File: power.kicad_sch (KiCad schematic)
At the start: 49 parts, among them IC1 STM32MP157AAB3, IC3 STC3117IJT, IC4 MCP73830T-2AAI_MYY, IC5 MT41K256M16TW-107_P, IC6 STPMIC1BPQR, P1 USB_C_Plug_USB2.0

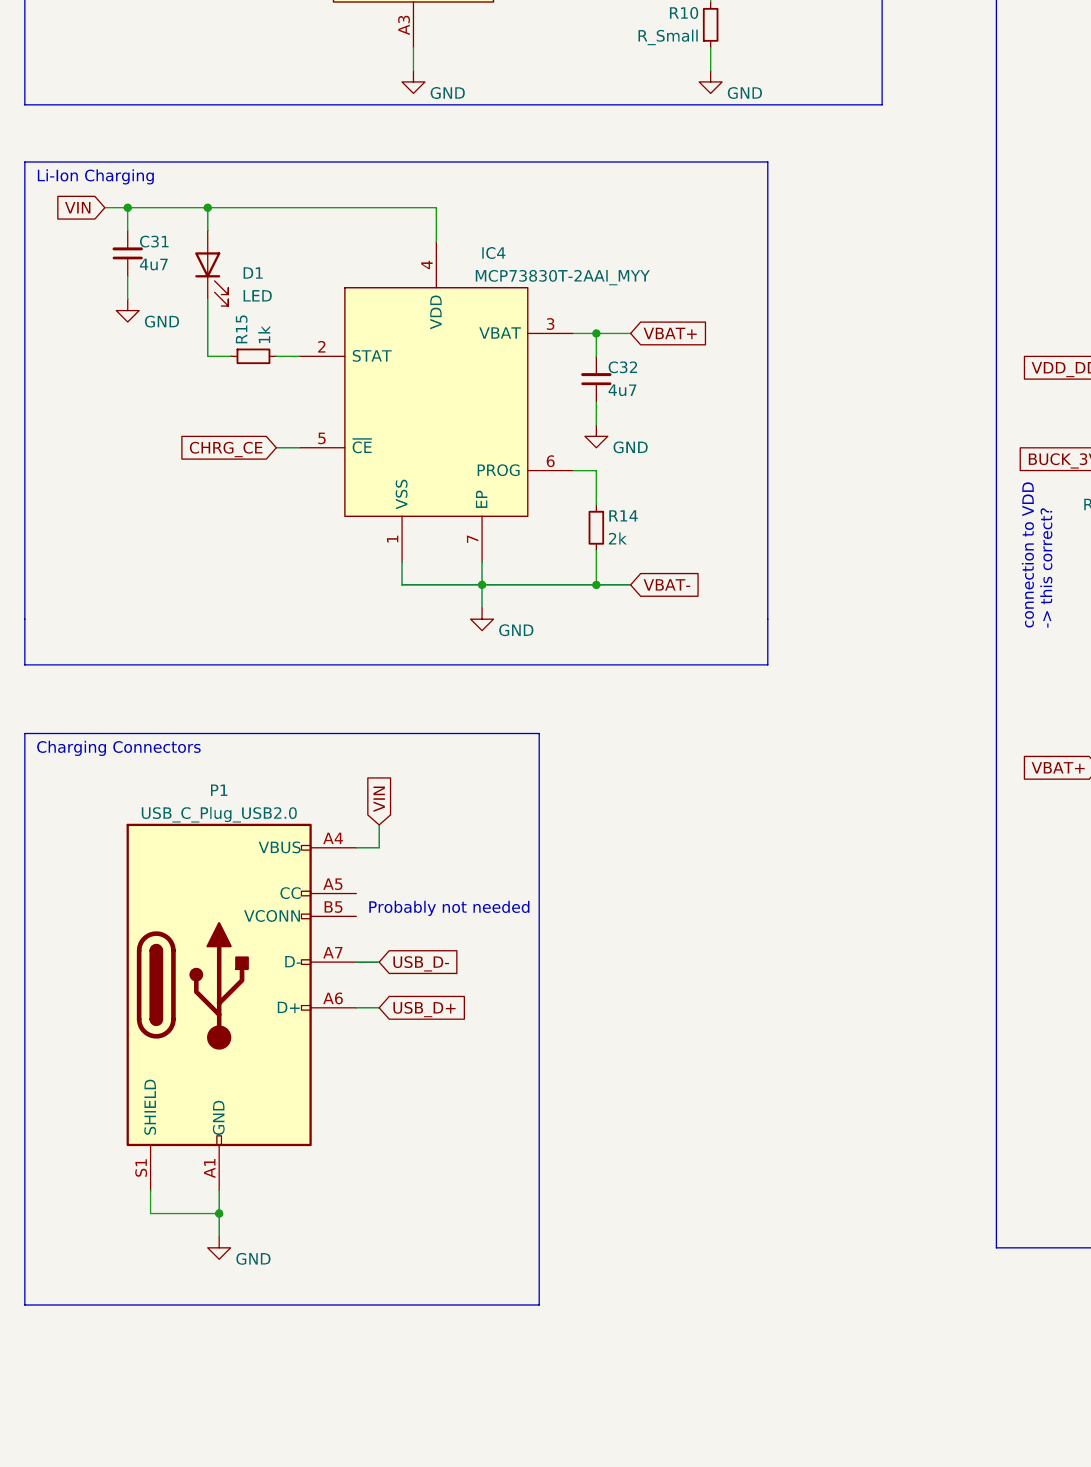
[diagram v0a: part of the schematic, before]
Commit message: Added Connectors
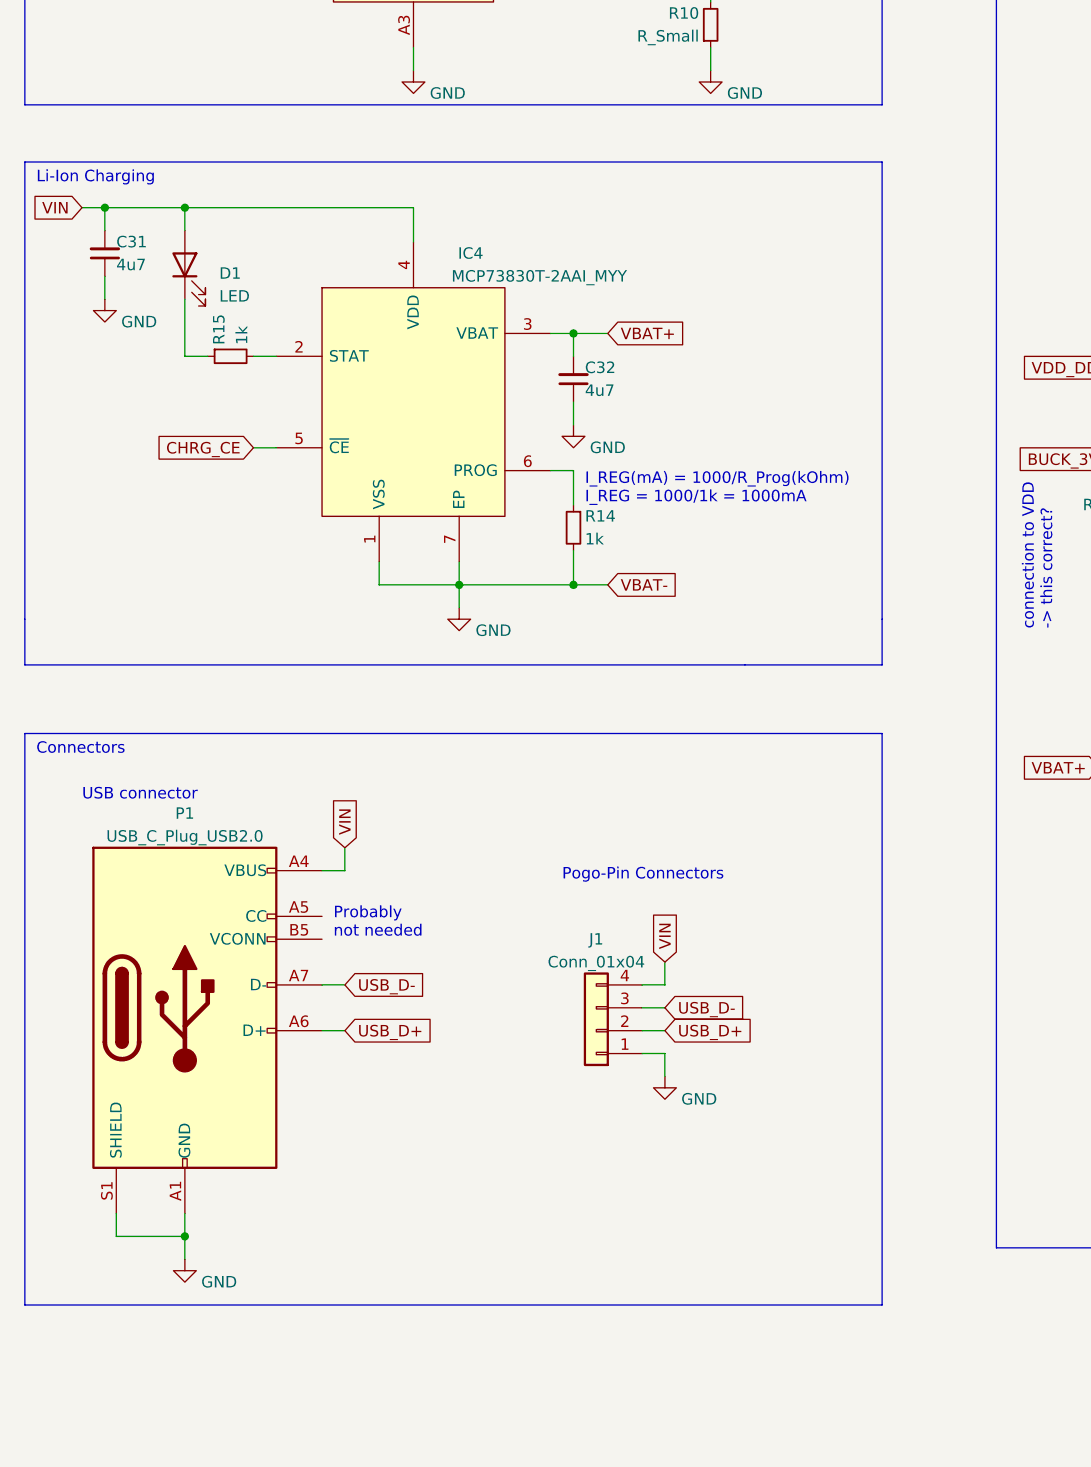
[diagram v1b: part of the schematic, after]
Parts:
- added J1: Conn_01x04, symbol Connector_Generic:Conn_01x04
- R14: value 2k -> 1k
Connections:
- net GND: now also J1.1 (Pin_1)
- net USB_D+: now also J1.2 (Pin_2)
- net USB_D-: now also J1.3 (Pin_3)
- net VIN: now also J1.4 (Pin_4)
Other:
- note added: "Connectors"
- note added: "I_REG(mA) = 1000/R_Prog(kOhm) I_REG = 1000/1k = 1000mA"
- note added: "Pogo-Pin Connectors"
- note added: "USB connector"
- note removed: "Charging Connectors"
- moved on the sheet: C31, C32, D1, IC4, P1, R14, R15

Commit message: Added STUSB1600A chip
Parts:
- added C33, C34, C35: 1u, Capacitor_SMD:C_0603_1608Metric, symbol Device:C_Small
- added C36: 10u, Capacitor_SMD:C_0603_1608Metric, symbol Device:C_Small
- added IC8: STUSB1600AQTR, ARMband:QFN50P400X400X100-25N, symbol ARMband:STUSB1600AQTR
- added R16, R18, R19, R22, R23, R24: 10k, Resistor_SMD:R_0603_1608Metric, symbol Device:R_Small
- added R17, R21: 1k, Resistor_SMD:R_0603_1608Metric, symbol Device:R_Small
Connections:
- net BUCK_3V3: now also C35.2, IC8.22 (VSYS), R18.2, R19.2, R22.2, R23.2, R24.2
- net GND: now also C33.1, C34.1, C35.1, C36.2, IC8.10 (GND), IC8.13 (ADDR0), IC8.25 (THERMAL_PAD), IC8.3 (VCONN), R21.2
- net SCL: now also IC8.7 (SCL)
- net SDA: now also IC8.8 (SDA)
- net VIN: now also C36.1, IC8.18 (VUS_SENSE)
- net USB_CC1: now reaches P1.A5 (CC)
- net USB_CC1: now also IC8.1 (CC1DB), IC8.2 (CC1)
- net USB_CC2: now reaches P1.B5 (VCONN)
- net USB_CC2: now also IC8.4 (CC2), IC8.5 (CC2DB)
- new net: R16.2, R17.1
- new net: IC8.19 (VBUS_EN_SNK), R17.2
- new net: C33.2, IC8.21 (VREG_1V2)
- new net: C34.2, IC8.23 (VREG_2V7)
- new net USB_ALERT#: IC8.9 (ALERT#), R23.1
- new net USB_ATTACH: IC8.12 (ATTACH), R19.1
- new net USB_A_B_SIDE: IC8.17 (A_B_SIDE), R24.1
- new net USB_DEBUG1: IC8.14 (DEBUG1), R18.1
- new net USB_RESET: IC8.6 (RESET), R21.1
- new net USB_VBUS_VALID: IC8.11 (VBUS_VALID), R22.1
- no-connect marks 0 -> 2
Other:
- note added: "STUSB in Sink application"
- note added: "TODO: dual PMOS"
- note added: "To GND/VIO"
- note added: "VIO: 3v3 or 1v8?"
- note added: "VSYS: power from system, connect to GND if not used"
- note removed: "Probably not needed"
- moved on the sheet: C10, C11, C12, C13, C14, C15, C16, C17, C18, C19, C20, C21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

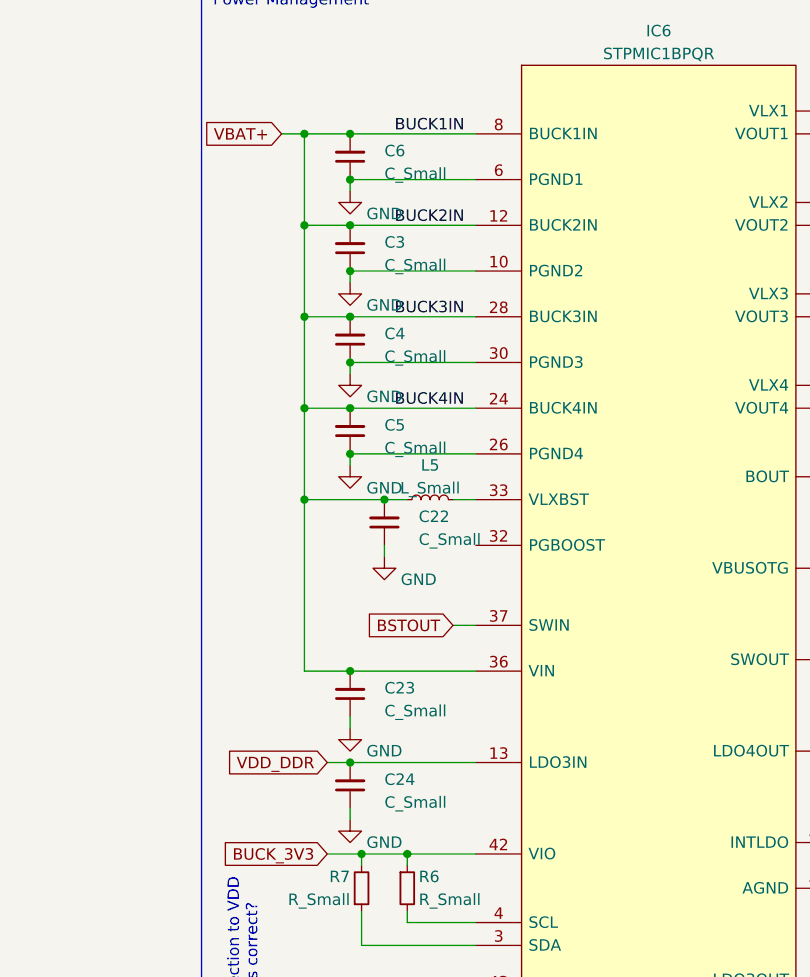
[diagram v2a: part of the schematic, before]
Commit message: added some part footprints
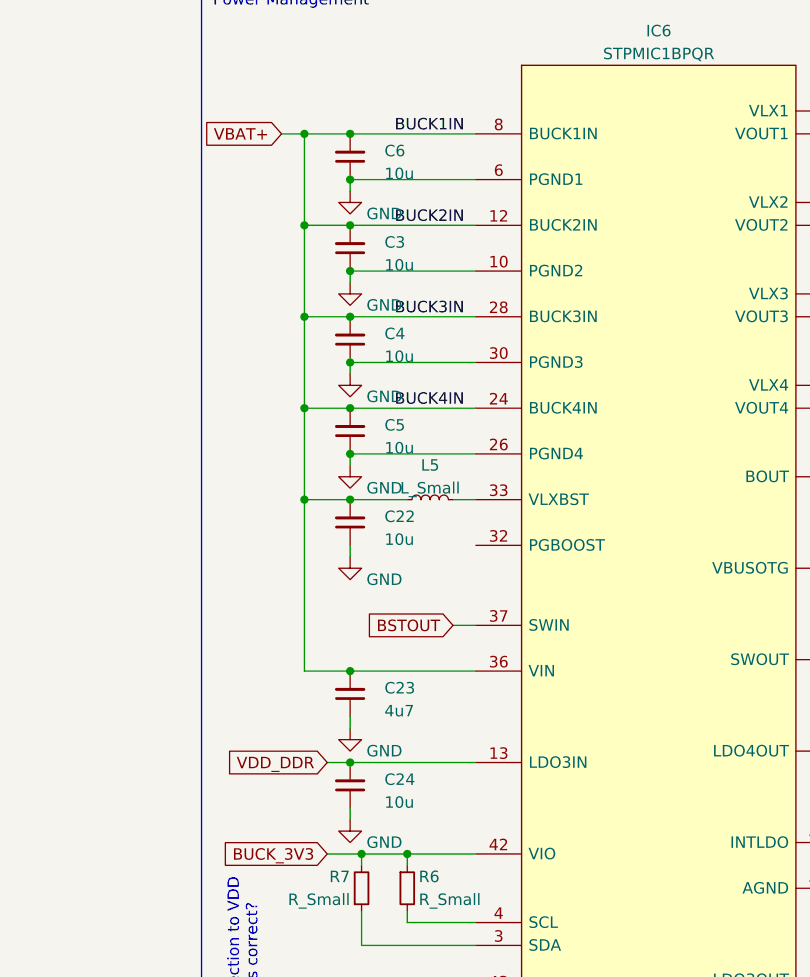
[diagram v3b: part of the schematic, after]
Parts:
- BT1: footprint (none) -> Connector_JST:JST_EH_S2B-EH_1x02_P2.50mm_Horizontal
- C22, C24: value C_Small -> 10u; footprint (none) -> Capacitor_SMD:C_0603_1608Metric
- C23: value C_Small -> 4u7
- C3, C4, C5, C6: value C_Small -> 10u; footprint (none) -> Capacitor_SMD:C_0603_1608Metric; MFN (none) -> 187-CL10A106MQ8NNNL

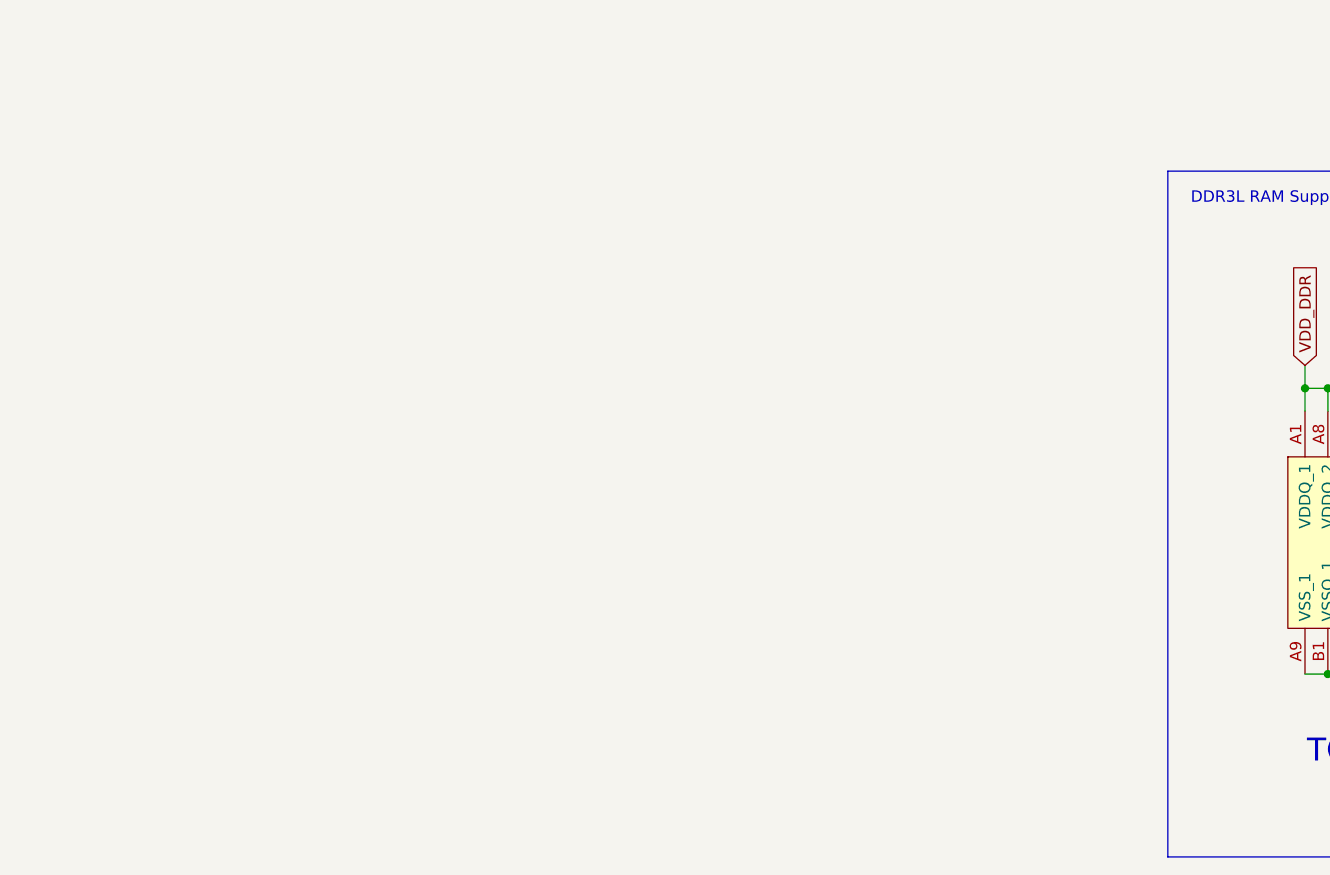
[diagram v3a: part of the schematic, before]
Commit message: Add Labels for DDR & DDR Power
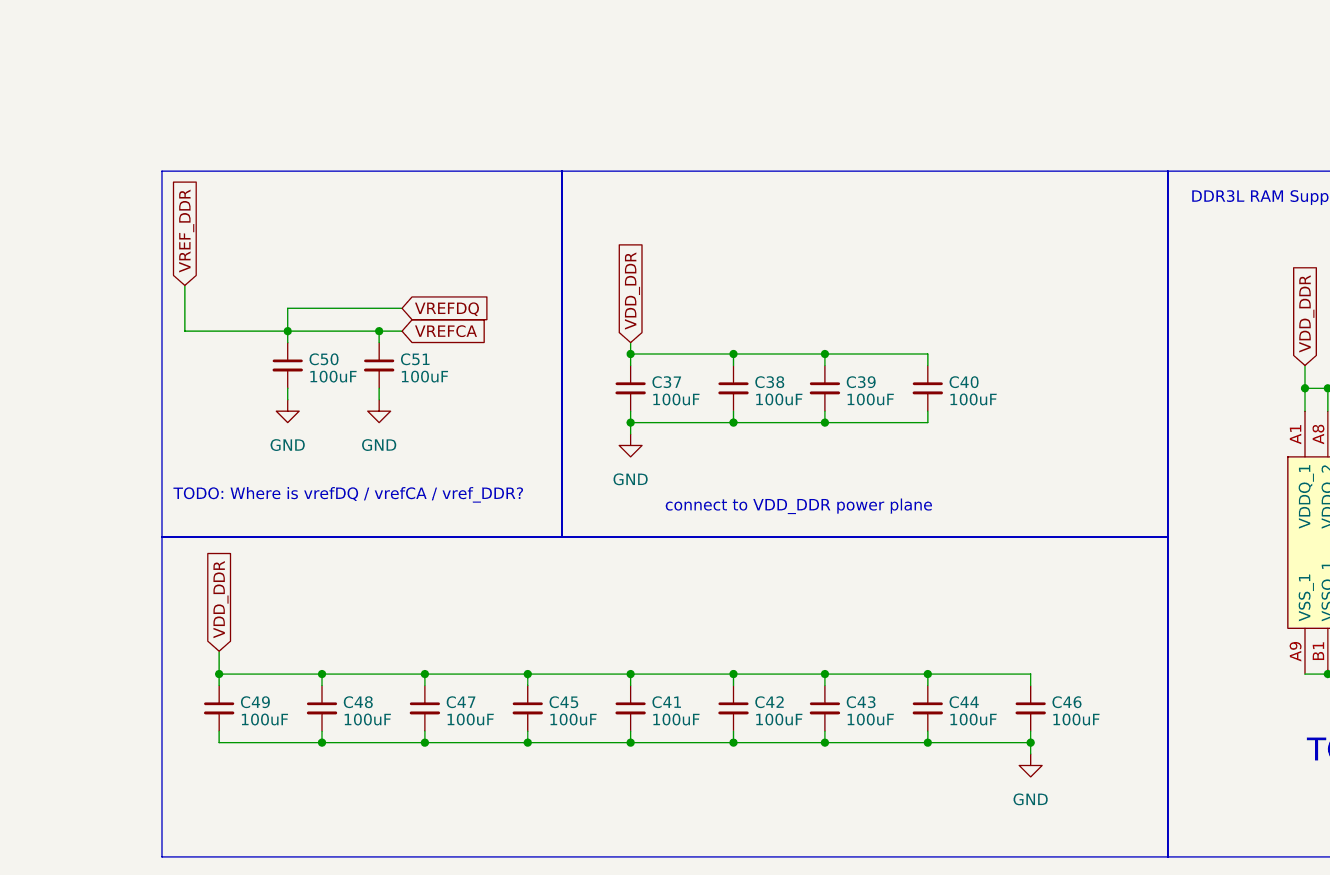
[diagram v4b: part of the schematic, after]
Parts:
- added C37, C38, C39, C40, C41, C42, C43, C44, C45, C46, C47, C48, C49, C50, C51: 100uF, symbol Device:C_Small
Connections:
- net GND: now also C37.2, C38.2, C39.2, C40.2, C41.2, C42.2, C43.2, C44.2, C45.2, C46.2, C47.2, C48.2, C49.2, C50.2, C51.2
- net VDD_DDR: now also C37.1, C38.1, C39.1, C40.1, C41.1, C42.1, C43.1, C44.1, C45.1, C46.1, C47.1, C48.1, C49.1
- net VREF_DDR renamed VREFCA
- net VREFCA: now also C50.1, C51.1
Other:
- note added: "TODO: Where is vrefDQ / vrefCA / vref_DDR?"
- note added: "connect to VDD_DDR power plane"
